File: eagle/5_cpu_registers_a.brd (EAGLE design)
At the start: 160 x 100 mm, 43 parts, among them IC1 74LS374N, IC10 74LS374N, IC11 74LS374N, IC12 74LS374N, IC13 74LS374N, IC14 74LS374N, IC2 74LS374N, IC21 74LS08N, IC22 74LS32N, IC3 74LS374N, IC4 74LS374N, IC5 74LS374N, IC6 74LS374N, IC7 74LS374N, IC8 74LS374N, IC9 74LS374N

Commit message: Removal of PPC started
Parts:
- removed C7, C8: 100n, rcl:C050-024X044
- removed IC7, IC8: 74LS374N, 74xx-eu:DIL20
- moved C5 65.6 mm to (70.5, 62.5)
- moved C3 45.4 mm to (83.2, 62.5)
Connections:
- removed net /ENPPC: IC7.1, IC8.1, JP9.37
- removed net /LDPPC: IC7.11, IC8.11, JP10.11
- net +5V: no longer C7.1, C8.1, IC7.20, IC8.20
- net ABUS0: no longer IC7.3
- net ABUS1: no longer IC7.4
- net ABUS10: no longer IC8.7
- net ABUS11: no longer IC8.8
- net ABUS12: no longer IC8.13
- net ABUS13: no longer IC8.14
- net ABUS14: no longer IC8.17
- net ABUS15: no longer IC8.18
- net ABUS2: no longer IC7.7
- net ABUS3: no longer IC7.8
- net ABUS4: no longer IC7.13
- net ABUS5: no longer IC7.14
- net ABUS6: no longer IC7.17
- net ABUS7: no longer IC7.18
- net ABUS8: no longer IC8.3
- net ABUS9: no longer IC8.4
- net GND: no longer C7.2, C8.2, IC7.10, IC8.10
- net RBUS0: no longer IC7.2
- net RBUS1: no longer IC7.5
- net RBUS10: no longer IC8.6
- net RBUS11: no longer IC8.9
- net RBUS12: no longer IC8.12
- net RBUS13: no longer IC8.15
- net RBUS14: no longer IC8.16
- net RBUS15: no longer IC8.19
- net RBUS2: no longer IC7.6
- net RBUS3: no longer IC7.9
- net RBUS4: no longer IC7.12
- net RBUS5: no longer IC7.15
- net RBUS6: no longer IC7.16
- net RBUS7: no longer IC7.19
- net RBUS8: no longer IC8.2
- net RBUS9: no longer IC8.5
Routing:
- net /ENPPC: track 285.8 -> 0.00 mm, vias 1 -> 0
- net /LDPPC: track 139.0 -> 0.00 mm, vias 2 -> 0
- net ABUS7: track 121.9 -> 36.6 mm
- net ABUS1: track 118.3 -> 41.5 mm
- net ABUS6: track 108.6 -> 33.9 mm, vias 1 -> 0
- net ABUS3: track 115.0 -> 41.2 mm
- net ABUS0: track 116.9 -> 44.5 mm
- net ABUS5: track 100.0 -> 33.9 mm
- net ABUS4: track 97.4 -> 33.9 mm
- net ABUS2: track 106.1 -> 43.5 mm
- net ABUS14: track 88.1 -> 33.9 mm
- net ABUS9: track 97.1 -> 68.4 mm
- net ABUS15: track 101.8 -> 78.9 mm
- net ABUS8: track 91.6 -> 71.6 mm, vias 1 -> 0
- net ABUS11: track 94.3 -> 77.3 mm
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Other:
- board text removed: "IC7"
- board text removed: "IC8"

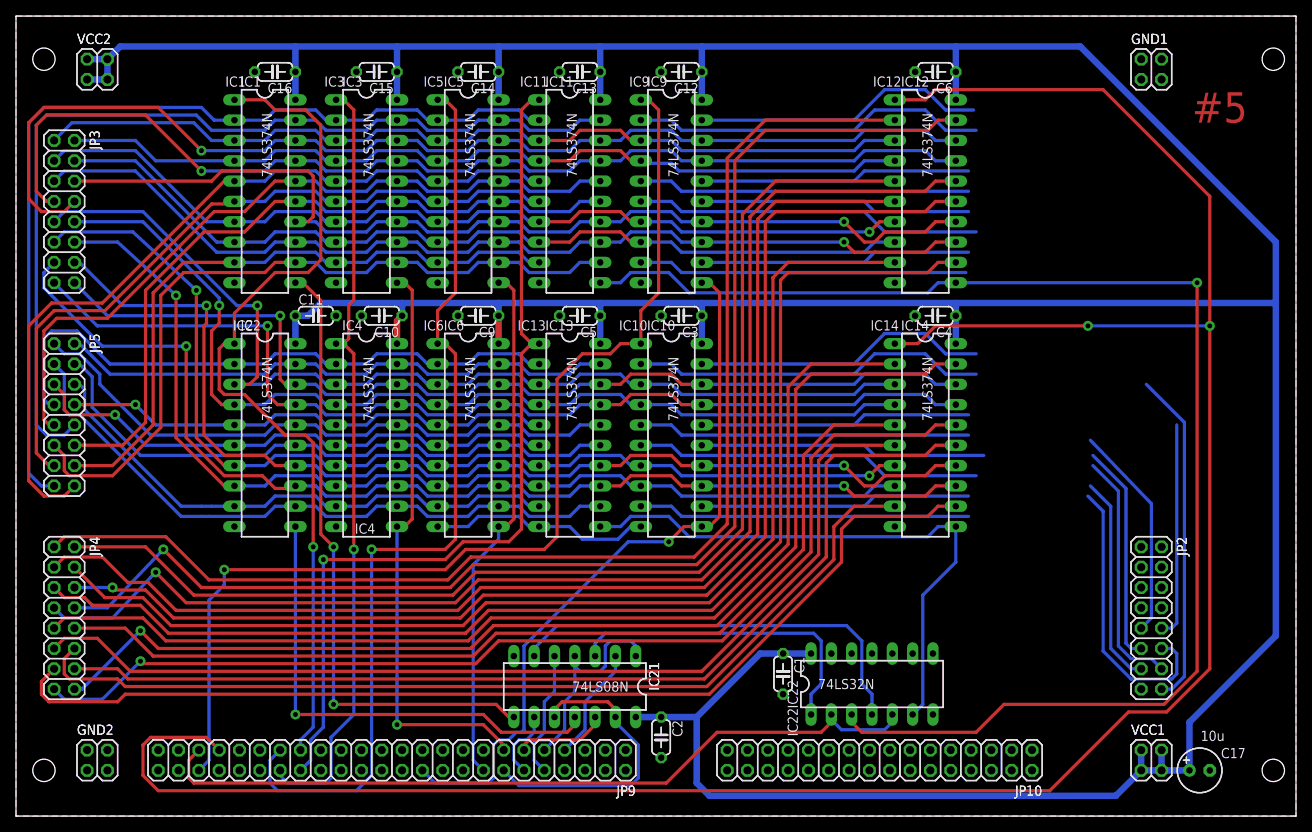
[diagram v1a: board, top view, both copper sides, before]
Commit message: PPC removal completed, control card RBUS selector changed from LS138 to LS139, removed /LDPPC and /ENPPC signals
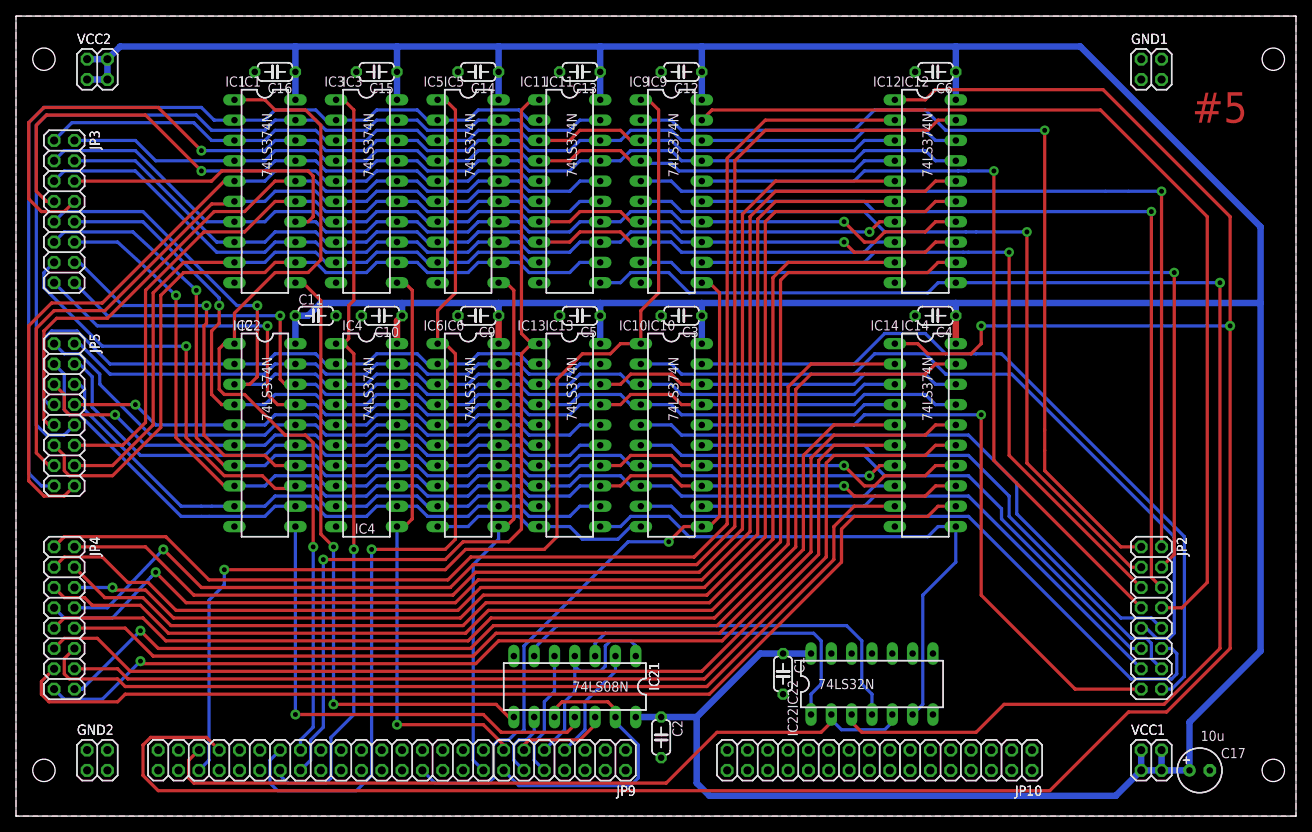
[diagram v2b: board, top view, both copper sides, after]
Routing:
- net ABUS7: track 36.6 -> 122.0 mm
- net ABUS5: track 33.9 -> 104.2 mm, vias 0 -> 1
- net ABUS1: track 41.5 -> 110.1 mm, vias 0 -> 1
- net ABUS0: track 44.5 -> 111.7 mm, vias 0 -> 1
- net ABUS6: track 33.9 -> 99.3 mm, vias 0 -> 1
- net ABUS3: track 41.2 -> 104.7 mm, vias 0 -> 1
- net ABUS2: track 43.5 -> 98.4 mm, vias 0 -> 1
- net ABUS4: track 33.9 -> 87.7 mm, vias 0 -> 1
- net ABUS14: track 33.9 -> 82.9 mm, vias 0 -> 1
- net ABUS8: track 71.6 -> 94.7 mm
- net ABUS15: track 78.9 -> 93.4 mm
- net ABUS9: track 68.4 -> 77.8 mm
- net /ENRMDR: track 299.6 -> 306.6 mm
- net ABUS13: track 66.2 -> 71.6 mm
- net ABUS12: track 60.1 -> 64.4 mm
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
